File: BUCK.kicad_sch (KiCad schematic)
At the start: 11 parts, among them U5 TPS562200

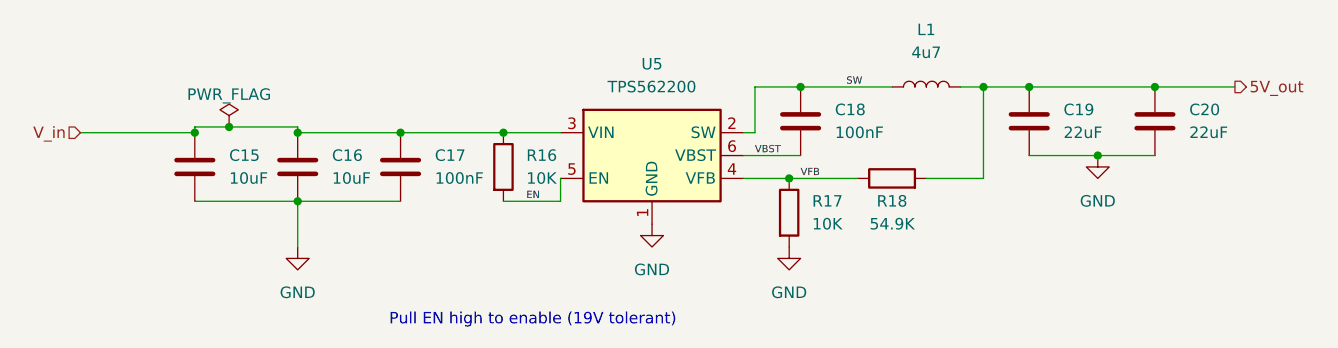
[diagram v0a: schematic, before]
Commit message: Added 0 Ω resistor to shield, grounded it, reannotated schematic, reassigned some footprints
Starting layout
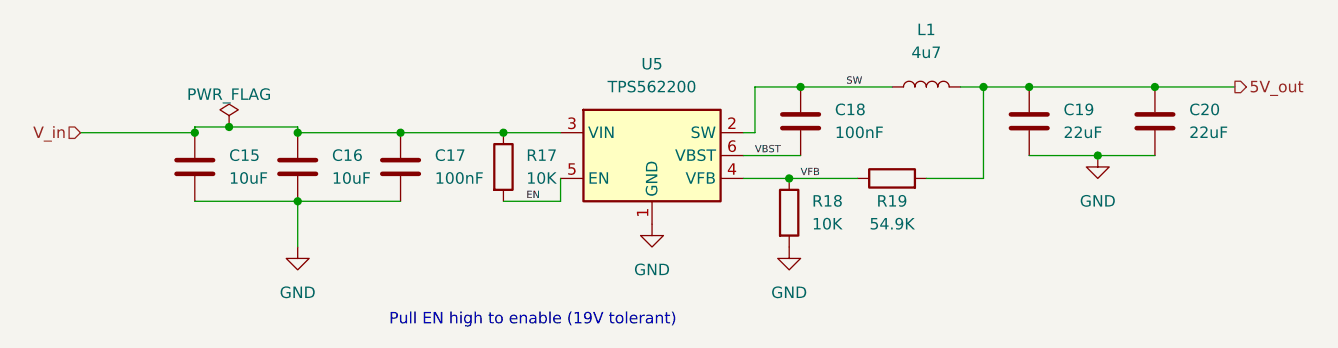
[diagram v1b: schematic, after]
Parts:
- renumbered R16 to R17, R17 to R18, R18 to R19
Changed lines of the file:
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@@
   (symbol (lib_id "power:GND") (at 193.04 81.915 0) (unit 1)
     (in_bom yes) (on_board yes) (fields_autoplaced)
-    (property "Reference" "#PWR048" (id 0) (at 193.04 88.265 0)
+    (property "Reference" "#PWR054" (id 0) (at 193.04 88.265 0)
       (effects (font (size 1.27 1.27)) hide)
     )
@@
   (symbol (lib_id "power:GND") (at 143.51 89.535 0) (unit 1)
     (in_bom yes) (on_board yes) (fields_autoplaced)
-    (property "Reference" "#PWR046" (id 0) (at 143.51 95.885 0)
+    (property "Reference" "#PWR052" (id 0) (at 143.51 95.885 0)
       (effects (font (size 1.27 1.27)) hide)
     )
@@
   (symbol (lib_id "Device:R") (at 170.18 84.455 90) (unit 1)
     (in_bom yes) (on_board yes)
-    (property "Reference" "R18" (id 0) (at 170.18 86.995 90))
+    (property "Reference" "R19" (id 0) (at 170.18 86.995 90))
     (property "Value" "54.9K" (id 1) (at 170.18 89.535 90))
     (property "Footprint" "Resistor_SMD:R_0603_1608Metric_Pad0.98x0.95mm_HandSolder" (id 2) (at 170.18 86.233 90)
@@
   (symbol (lib_id "Device:R") (at 127 83.185 0) (unit 1)
     (in_bom yes) (on_board yes) (fields_autoplaced)
-    (property "Reference" "R16" (id 0) (at 129.54 81.9149 0)
+    (property "Reference" "R17" (id 0) (at 129.54 81.9149 0)
       (effects (font (size 1.27 1.27)) (justify left))
     )
@@
   (symbol (lib_id "power:GND") (at 158.75 92.075 0) (unit 1)
     (in_bom yes) (on_board yes) (fields_autoplaced)
-    (property "Reference" "#PWR047" (id 0) (at 158.75 98.425 0)
+    (property "Reference" "#PWR053" (id 0) (at 158.75 98.425 0)
       (effects (font (size 1.27 1.27)) hide)
     )
@@
   (symbol (lib_id "Device:R") (at 158.75 88.265 0) (unit 1)
     (in_bom yes) (on_board yes) (fields_autoplaced)
-    (property "Reference" "R17" (id 0) (at 161.29 86.9949 0)
+    (property "Reference" "R18" (id 0) (at 161.29 86.9949 0)
       (effects (font (size 1.27 1.27)) (justify left))
     )
@@
   (symbol (lib_id "power:GND") (at 104.14 92.075 0) (unit 1)
     (in_bom yes) (on_board yes) (fields_autoplaced)
-    (property "Reference" "#PWR045" (id 0) (at 104.14 98.425 0)
-      (effects (font (size 1.27 1.27)) hide)
-    )
+    (property "Reference" "#PWR051" (id 0) (at 104.14 98.425 0)
+      (effects (font (size 1.27 1.27)) hide)
+    )
